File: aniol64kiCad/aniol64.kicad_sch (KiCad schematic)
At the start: 32 parts, among them J1 RST, J2 PWR, U12 74LS74, U2 74LS14, U4 74LS32, U5 74LS08, U6 74LS02, X1 ACO-1.8432MHz

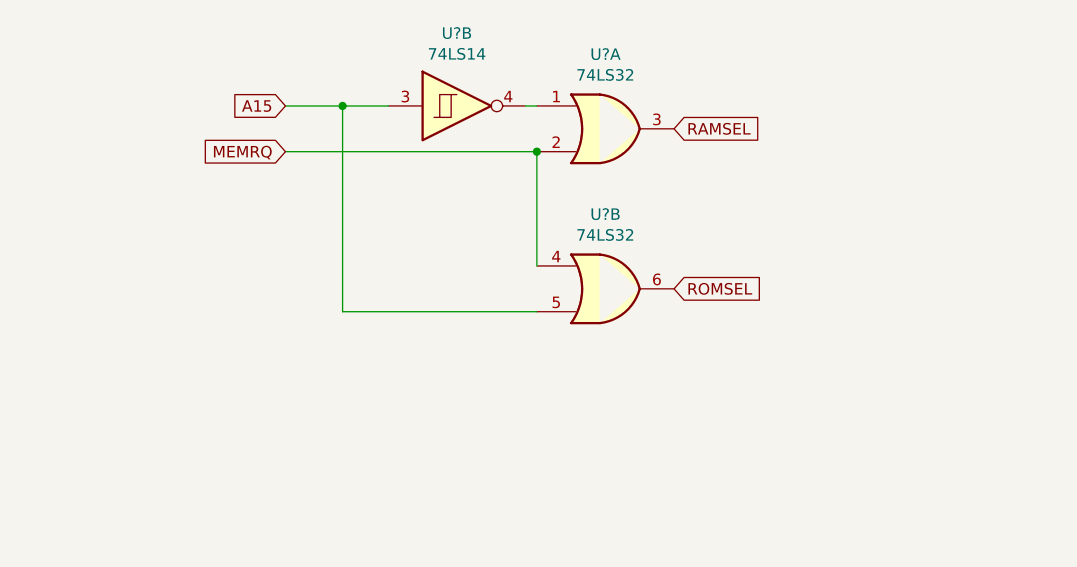
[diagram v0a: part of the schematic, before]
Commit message: added scrolling in edit
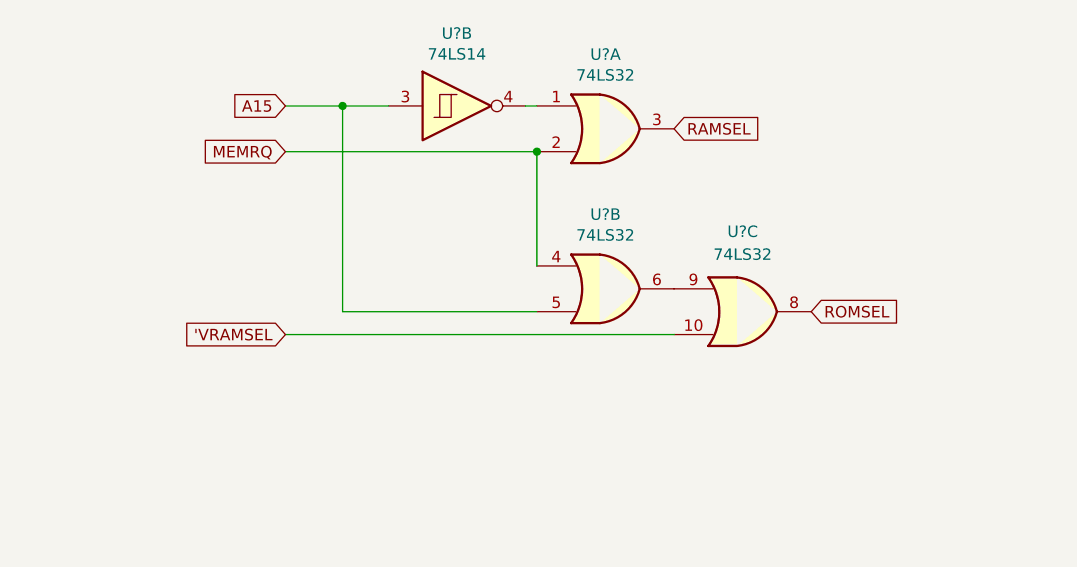
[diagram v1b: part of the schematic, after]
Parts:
- added U?: 74LS32, symbol 74xx:74LS32
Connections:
- net ROMSEL: now also U?.8; no longer U?.6
- new net: U?.6, U?.9
- new net 'VRAMSEL: U?.10
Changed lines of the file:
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@@
+    (stroke (width 0) (type default) (color 0 0 0 0))
+  )
+  (wire (pts (xy 151.13 139.7) (xy 194.31 139.7))
     (stroke (width 0) (type default) (color 0 0 0 0))
   )
@@
     )
   )
+  (global_label "'VRAMSEL" (shape input) (at 151.13 139.7 180) (fields_autoplaced)
+    (effects (font (size 1.27 1.27)) (justify right))
+    (property "Intersheet References" "${INTERSHEET_REFS}" (id 0) (at 139.9158 139.6206 0)
+      (effects (font (size 1.27 1.27)) (justify right) hide)
+    )
+  )
   (global_label "A9" (shape input) (at 201.93 72.39 180) (fields_autoplaced)
     (effects (font (size 1.27 1.27)) (justify right))
@@
     )
   )
-  (global_label "ROMSEL" (shape input) (at 194.31 134.62 0) (fields_autoplaced)
-    (effects (font (size 1.27 1.27)) (justify left))
-    (property "Intersheet References" "${INTERSHEET_REFS}" (id 0) (at 0 0 0)
+  (global_label "ROMSEL" (shape input) (at 209.55 137.16 0) (fields_autoplaced)
+    (effects (font (size 1.27 1.27)) (justify left))
+    (property "Intersheet References" "${INTERSHEET_REFS}" (id 0) (at 15.24 2.54 0)
       (effects (font (size 1.27 1.27)) hide)
     )
@@
     (pin "7")
   )
+  (symbol (lib_id "74xx:74LS32") (at 201.93 137.16 0) (unit 3)
+    (in_bom yes) (on_board yes) (fields_autoplaced)
+    (property "Reference" "U?" (id 0) (at 201.93 128.27 0))
+    (property "Value" "74LS32" (id 1) (at 201.93 130.81 0))
+    (property "Footprint" "" (id 2) (at 201.93 137.16 0)
+      (effects (font (size 1.27 1.27)) hide)
+    )
+    (property "Datasheet" "http://www.ti.com/lit/gpn/sn74LS32" (id 3) (at 201.93 137.16 0)
+      (effects (font (size 1.27 1.27)) hide)
+    )
+    (pin "1")
+    (pin "2")
+    (pin "3")
+    (pin "4")
+    (pin "5")
+    (pin "6")
+    (pin "10")
+    (pin "8")
+    (pin "9")
+    (pin "11")
+    (pin "12")
+    (pin "13")
+    (pin "14")
+    (pin "7")
+  )
   (sheet (at 30.48 58.42) (size 12.7 3.81) (fields_autoplaced)
     (stroke (width 0) (type solid) (color 0 0 0 0))
@@
       (reference "U?") (unit 3) (value "74LS14") (footprint "")
     )
+    (path "/086dc200-070f-4ed6-ba4a-f5ff252d3173"
+      (reference "U?") (unit 3) (value "74LS32") (footprint "")
+    )
     (path "/00000000-0000-0000-0000-000061d3d043"
